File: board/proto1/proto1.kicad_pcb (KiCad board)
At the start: 2 copper layers, 120 x 70 mm, 28 parts, among them J1 CONN_01X10, J2 CONN_01X10, SW1 SW_PUSH, U1 LM7805CT, U2 74LS04, U3 74LS244, U4 74LS374, U5 74LS139, U6 Z80CPU, U7 27C64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

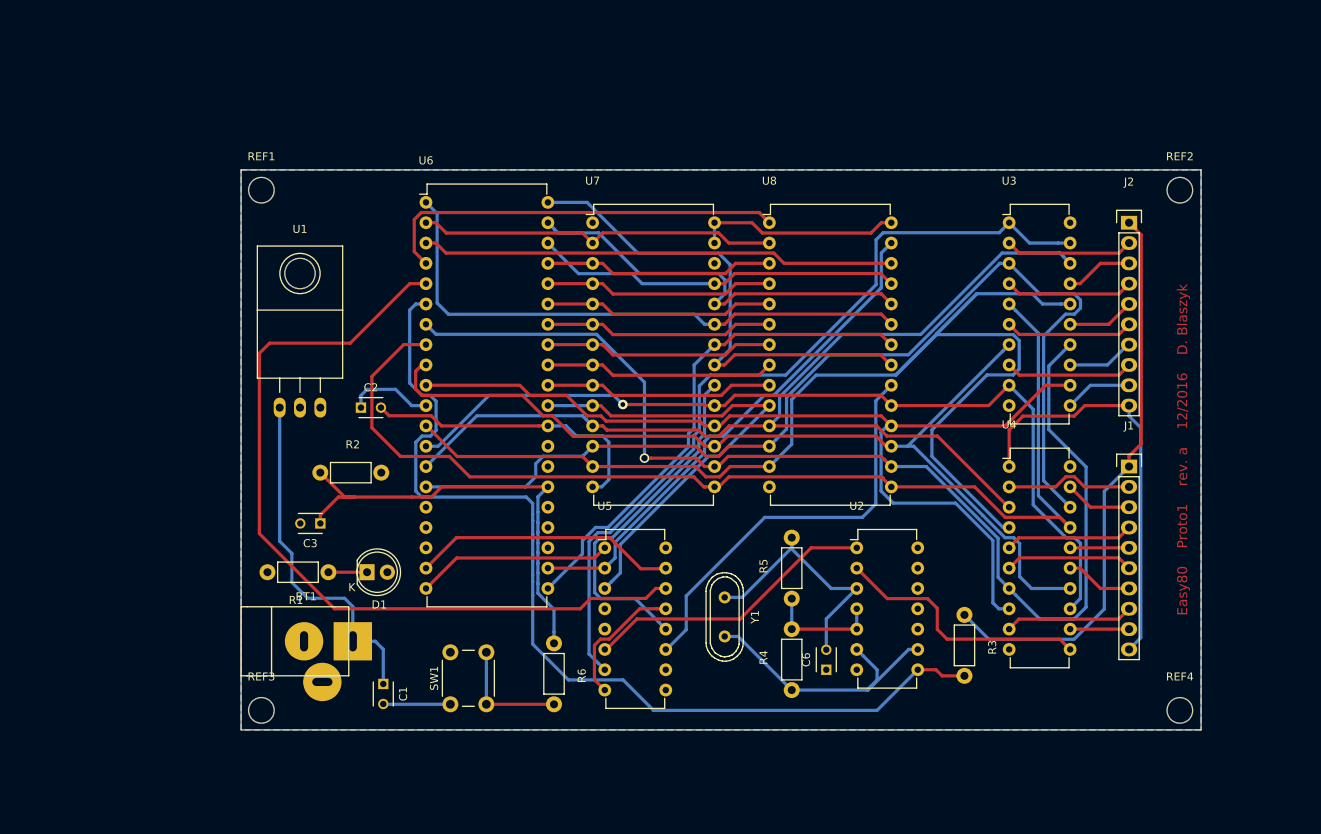
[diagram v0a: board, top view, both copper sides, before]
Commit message: some small improvements in the tracks removed some redundant tracks recreated the PDF's
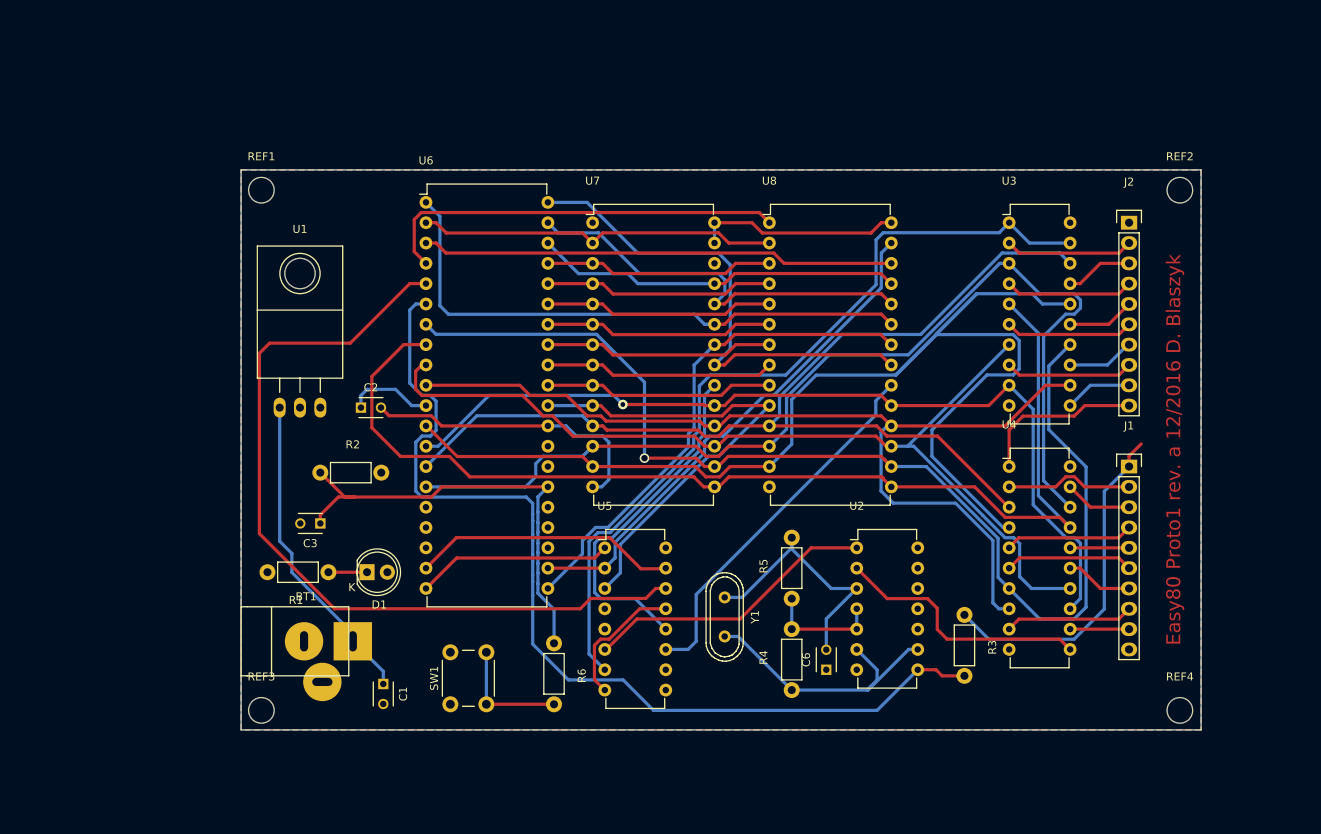
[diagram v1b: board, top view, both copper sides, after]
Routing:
- net GND: track 116.7 -> 76.6 mm
- net VCC: track 109.1 -> 80.8 mm
- net ramcs: track 51.9 -> 46.3 mm
- net Net-(BT1-Pad1): track 44.2 -> 39.9 mm

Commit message: update board to eurocard size (160x100mm) and re-layout
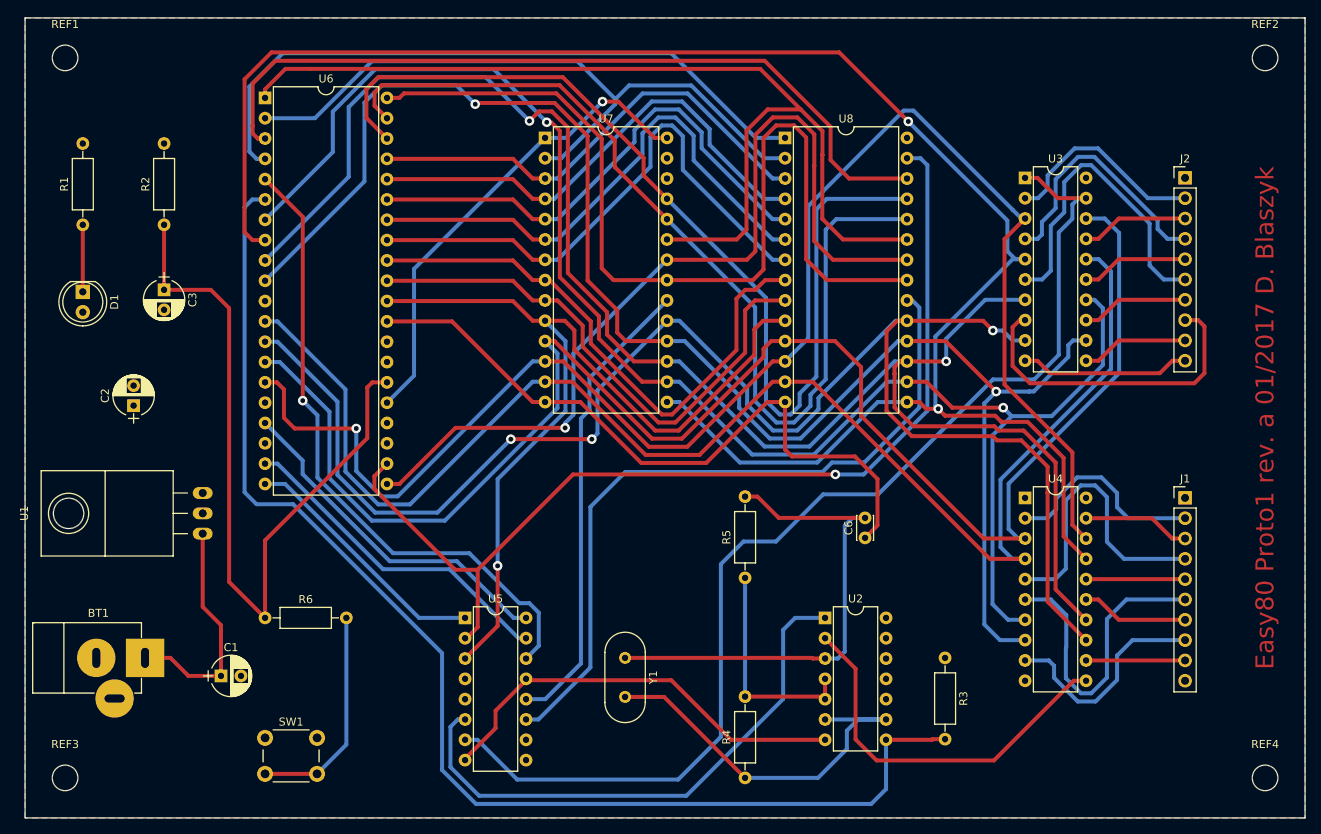
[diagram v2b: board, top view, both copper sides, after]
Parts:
- C1, C2, C3: footprint Capacitors_ThroughHole:C_Disc_D3_P2.5 -> Capacitors_ThroughHole:CP_Radial_D5.0mm_P2.50mm
- C6: footprint Capacitors_ThroughHole:C_Disc_D3_P2.5 -> Capacitors_ThroughHole:C_Disc_D3.0mm_W2.0mm_P2.50mm
- D1: footprint LEDs:LED-5MM -> LEDs:LED_D5.0mm
- J1, J2: footprint Pin_Headers:Pin_Header_Straight_1x10 -> Pin_Headers:Pin_Header_Straight_1x10_Pitch2.54mm
- R1, R2, R3, R4, R5, R6: footprint Resistors_ThroughHole:Resistor_Horizontal_RM7mm -> Resistors_ThroughHole:R_Axial_DIN0207_L6.3mm_D2.5mm_P10.16mm_Horizontal
- SW1: value SW_PUSH -> SW_Push
- moved R1 53.2 mm to (77.2, 70.9), turned to 90 degrees
- moved D1 49.9 mm to (77.2, 79.2), turned to 270 degrees
- moved R2 36.6 mm to (87.4, 70.9), turned to 90 degrees
- moved R6 36.3 mm to (100.0, 120.0), turned to 0 degrees
- moved C3 35.1 mm to (87.4, 79.0), turned to 270 degrees
- moved REF1 29.6 mm to (75.0, 50.0)
- moved C2 28.4 mm to (83.6, 93.5), turned to 90 degrees
- moved REF3 25.9 mm to (75.0, 140.0)
- moved U6 24.0 mm to (100.0, 55.0)
- moved SW1 23.5 mm to (100.0, 135.0), turned to 0 degrees
- moved C1 20.3 mm to (94.5, 127.3), turned to 0 degrees
- moved BT1 20.0 mm to (85.0, 125.0)
- moved REF2 19.7 mm to (225.0, 50.0)
- moved U5 19.5 mm to (125.0, 120.0)
- moved U1 18.0 mm to (92.2, 106.9), turned to 90 degrees
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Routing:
- net /D3: track 139.4 -> 230.9 mm, vias 0 -> 2
- net GND: track 76.6 -> 162.3 mm
- net /D7: track 111.0 -> 196.4 mm, vias 1 -> 3
- net /D5: track 117.4 -> 202.4 mm, vias 0 -> 2
- net /A8: track 46.1 -> 126.0 mm
- net /D6: track 121.4 -> 197.0 mm, vias 0 -> 2
- net /D0: track 129.8 -> 200.4 mm
- net /A9: track 51.8 -> 119.4 mm
- net /D1: track 129.4 -> 196.0 mm, vias 0 -> 1
- net wr: track 64.3 -> 128.3 mm, vias 0 -> 1
- net /A10: track 62.5 -> 119.3 mm
- net /A11: track 72.1 -> 128.4 mm
- net /A0: track 60.9 -> 114.3 mm, vias 0 -> 1
- net /D4: track 143.7 -> 195.0 mm, vias 1 -> 2
- net rd: track 63.2 -> 112.6 mm, vias 0 -> 1
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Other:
- board size 120 x 70 mm -> 160 x 100 mm
- net class Default: clearance 0.25 -> 0.5; trace_width 0.4 -> 0.5
- rule trace_clearance: 0.25 -> 0.5
- board text added: "Easy80 Proto1 rev. a 01/2017 D. Blaszyk"
- board text removed: "Easy80 Proto1 rev. a 12/2016 D. Blaszyk"
